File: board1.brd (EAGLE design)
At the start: 40 x 30 mm, 7 parts

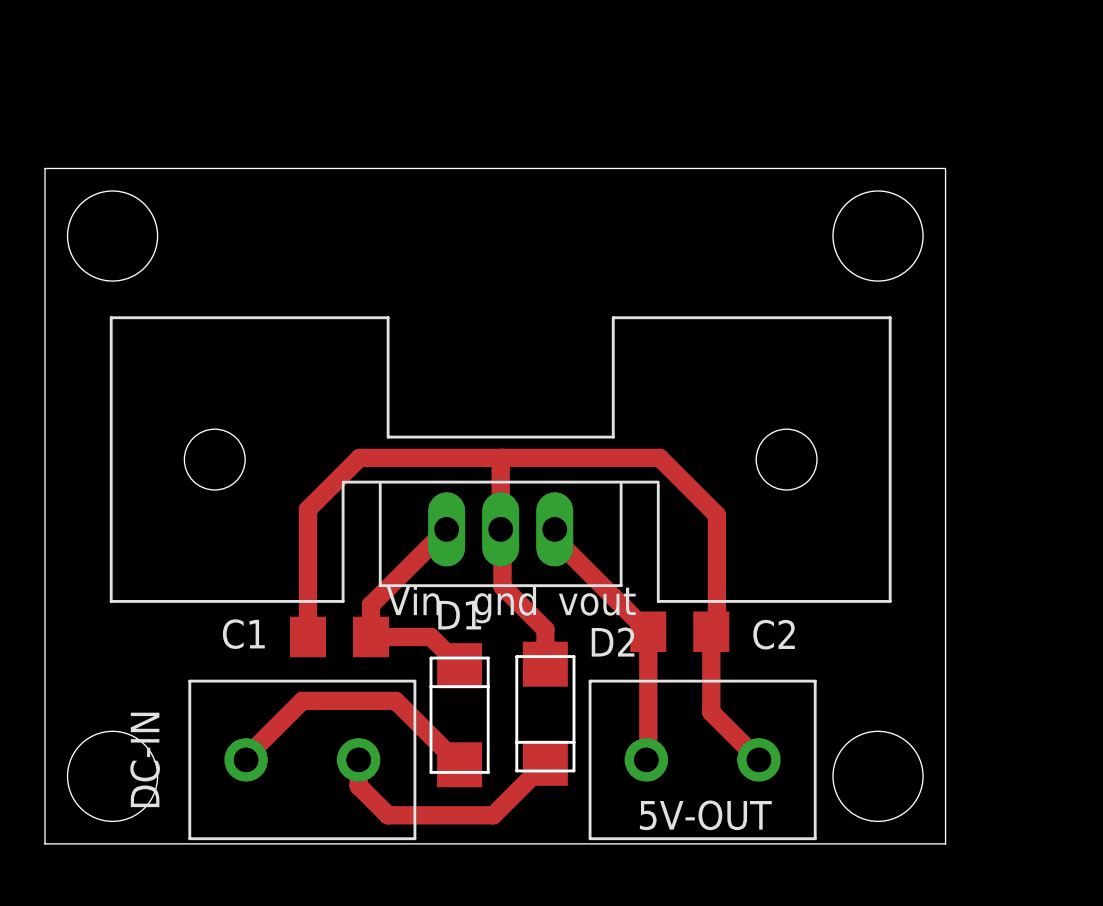
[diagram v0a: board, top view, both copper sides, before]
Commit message: Final version. Added also vias for soldering external the sensor (maybe we will remove them)
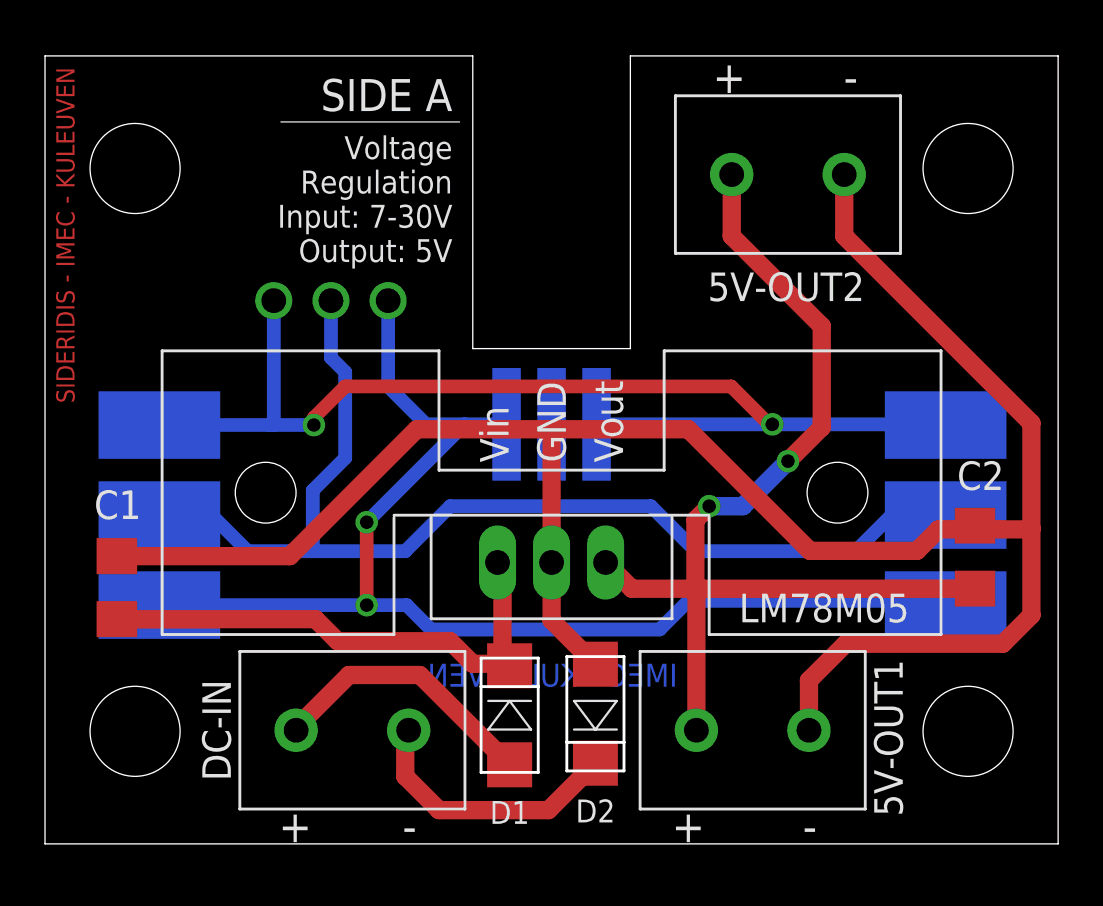
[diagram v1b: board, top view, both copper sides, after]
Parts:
- removed 5V-OUT: 2PIN-TERMINAL-5MMPITCH, Paschalis_connectors:2PIN-TERMINAL-5MMPITCH
- removed U$3: LM78M05, Bart_educatief_aanbod:LM78M05_PAC
- added 5V-OUT1, 5V-OUT2: 2PIN-TERMINAL-5MMPITCH, Paschalis_connectors:2PIN-TERMINAL-5MMPITCH
- added BUS1, BUS2: AVX-3PIN-SMD-CON, Paschalis_connectors:AVX-3PIN-SMD-CON
- added DS18B20: SMD-3PAD-DS18B20, Paschalis_connectors:SMD-3PAD-DS18B20
- added LM78M05: LM78M05, Bart_educatief_aanbod:LM78M05_PAC
- moved C2 13.5 mm to (41.3, 12.7), turned to 90 degrees
- moved C1 10.1 mm to (3.19, 11.4), turned to 90 degrees
- moved DC-IN 2.58 mm to (13.7, 5.05)
- moved D1 2.22 mm to (20.6, 5.71)
- moved D2 2.22 mm to (24.4, 5.78)
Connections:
- net N$1 renamed VIN
- removed net N$3: 5V-OUT.2, C1.2, C2.2, D2.P$1, U$3.2
- removed net N$5: 5V-OUT.1, C2.1, U$3.3
- new net 5V: 5V-OUT1.1, 5V-OUT2.1, C2.1, LM78M05.3
- new net GND: 5V-OUT1.2, 5V-OUT2.2, C1.2, C2.2, D2.P$1, LM78M05.2
- new net S_DQ: BUS1.P$2, BUS2.P$2, DS18B20.P$2
- new net S_GND: BUS1.P$1, BUS2.P$1, DS18B20.P$1
- new net S_VDD: BUS1.P$3, BUS2.P$3, DS18B20.P$3
- net N$2: now also LM78M05.1; no longer U$3.1
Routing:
- net GND: track 0.00 -> 93.4 mm
- net S_VDD: track 0.00 -> 55.6 mm, vias 0 -> 3
- net S_DQ: track 0.00 -> 53.6 mm, vias 0 -> 1
- net S_GND: track 0.00 -> 49.9 mm, vias 0 -> 3
- net N$3: track 47.7 -> 0.00 mm
- net 5V: track 0.00 -> 46.5 mm, vias 0 -> 2
- net N$2: track 10.6 -> 23.1 mm
- net N$5: track 12.0 -> 0.00 mm
- net N$4: track 10.9 -> 12.0 mm
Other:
- board size 40 x 30 mm -> 45 x 35 mm
- board text added: "+"
- board text added: "-"
- board text added: "5V"
- board text added: "Address"
- board text added: "DQ"
- board text added: "GND"
- board text added: "IMEC - KULEUVEN"
- board text added: "LM78M05"
- board text added: "Paschalis Sideridis April 2016"
- board text added: "SIDE A"
- board text added: "SIDE B"
- board text added: "SIDERIDIS - IMEC - KULEUVEN"
- board text added: "Temperature 1Wire BUS DS18B20"
- board text added: "Voltage Regulation Input: 7-30V Output: 5V"

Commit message: Removed the vias. Simple design, version v1.0
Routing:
- net S_DQ: track 53.6 -> 41.6 mm, vias 1 -> 0
- net S_VDD: track 55.6 -> 47.7 mm, vias 3 -> 2
- net S_GND: track 49.9 -> 44.4 mm, vias 3 -> 2
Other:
- board text added: "Paschalis Sideridis April 2016 v1.0"
- board text removed: "Paschalis Sideridis April 2016"
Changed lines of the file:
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@@
 <text x="43.4975" y="10.4775" size="1.016" layer="26" font="vector" rot="MR90" align="bottom-center">GND</text>
 <text x="26.78" y="34.4725" size="1.016" layer="26" font="vector" rot="MR0" align="top-right">Paschalis Sideridis
-April 2016</text>
+April 2016 v1.0</text>
 <text x="22.5425" y="6.985" size="1.016" layer="16" font="vector" rot="MR0" align="bottom-center">IMEC - KULEUVEN</text>
 <dimension x1="0" y1="35" x2="19" y2="35" x3="9.5" y3="37" textsize="0.6096" layer="47" width="0.03"/>
@@
 <wire x1="32.305340625" y1="18.635" x2="39.975" y2="18.635" width="0.6096" layer="16"/>
 <wire x1="39.975" y1="18.635" x2="40.005" y2="18.605" width="0.6096" layer="16"/>
-<wire x1="5.08" y1="18.605" x2="9.962546875" y2="18.605" width="0.6096" layer="16"/>
-<wire x1="10.16" y1="18.605" x2="11.94251875" y2="18.605" width="0.6096" layer="16"/>
+<wire x1="5.08" y1="18.605" x2="11.94251875" y2="18.605" width="0.6096" layer="16"/>
 <wire x1="24.47" y1="18.605" x2="24.5" y2="18.635" width="0.6096" layer="16"/>
 <via x="11.94251875" y="18.605" extent="1-16" drill="0.6"/>
@@
 <wire x1="32.305340625" y1="18.635" x2="32.165" y2="18.635" width="0.6096" layer="1"/>
 <wire x1="32.165" y1="18.635" x2="30.48" y2="20.32" width="0.6096" layer="1"/>
-<via x="10.16" y="24.13" extent="1-16" drill="1.1"/>
-<wire x1="9.962546875" y1="18.605" x2="10.16" y2="18.605" width="0.6096" layer="16"/>
-<wire x1="10.16" y1="18.605" x2="10.16" y2="24.13" width="0.6096" layer="16"/>
 </signal>
 <signal name="S_DQ">
@@
 <wire x1="5.08" y1="14.605" x2="7.395" y2="14.605" width="0.6096" layer="16"/>
 <wire x1="7.395" y1="14.605" x2="9" y2="13" width="0.6096" layer="16"/>
-<wire x1="9" y1="13" x2="11.892228125" y2="13" width="0.6096" layer="16"/>
-<wire x1="11.892228125" y1="13" x2="16" y2="13" width="0.6096" layer="16"/>
+<wire x1="9" y1="13" x2="16" y2="13" width="0.6096" layer="16"/>
 <wire x1="16" y1="13" x2="18" y2="15" width="0.6096" layer="16"/>
 <wire x1="40.005" y1="14.605" x2="37.605" y2="14.605" width="0.6096" layer="16"/>
@@
 <wire x1="36" y1="13" x2="28.91" y2="13" width="0.6096" layer="16"/>
 <wire x1="28.91" y1="13" x2="26.91" y2="15" width="0.6096" layer="16"/>
-<via x="12.7" y="24.13" extent="1-16" drill="1.1"/>
-<wire x1="11.892228125" y1="13" x2="11.892228125" y2="15.702228125" width="0.6096" layer="16"/>
-<wire x1="11.892228125" y1="15.702228125" x2="13.335" y2="17.145" width="0.6096" layer="16"/>
-<wire x1="13.335" y1="17.145" x2="13.335" y2="20.955" width="0.6096" layer="16"/>
-<wire x1="13.335" y1="20.955" x2="12.7" y2="21.59" width="0.6096" layer="16"/>
-<wire x1="12.7" y1="21.59" x2="12.7" y2="24.13" width="0.6096" layer="16"/>
 </signal>
 <signal name="S_VDD">
@@
 <wire x1="14.2875" y1="14.2875" x2="14.2875" y2="10.605" width="0.6096" layer="1"/>
 <via x="14.2875" y="10.605" extent="1-16" drill="0.6"/>
-<via x="15.24" y="24.13" extent="1-16" drill="1.1"/>
-<wire x1="18.635" y1="18.635" x2="16.925" y2="18.635" width="0.6096" layer="16"/>
-<wire x1="16.925" y1="18.635" x2="15.24" y2="20.32" width="0.6096" layer="16"/>
-<wire x1="15.24" y1="20.32" x2="15.24" y2="24.13" width="0.6096" layer="16"/>
 </signal>
 </signals>
